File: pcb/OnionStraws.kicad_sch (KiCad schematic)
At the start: 33 parts, among them J1 8P8C, Q1 Si2393DS

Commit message: Updated PCB
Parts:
- C2: value 10u -> 100u
- C3: value 100n -> 1u
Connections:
- net GEA_HalfDplx: now also D?.2 (A); no longer D?.1 (K)
- net at R6.1, U?.12 (B2): now also D?.1 (K); no longer D?.2 (A)
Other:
- note added: "Add voltage supervisor to hold ESP reset until power is good."
- note added: "FullRX & TX not tested"
- moved on the sheet: D?
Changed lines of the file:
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@@
     (stroke (width 0) (type default) (color 0 0 0 0))
+  )
+  (text "Add voltage supervisor to hold ESP reset until power is good."
+    (at 85.725 191.77 0)
+    (effects (font (size 1.27 1.27)) (justify left bottom))
   )
   (text "EN" (at 256.54 35.56 0)
@@
   )
   (text "VI" (at 256.54 33.02 0)
+    (effects (font (size 1.27 1.27)) (justify left bottom))
+  )
+  (text "FullRX & TX not tested" (at 85.725 186.055 0)
     (effects (font (size 1.27 1.27)) (justify left bottom))
   )
@@
       (effects (font (size 1.27 1.27)) (justify left))
     )
-    (property "Value" "10u" (id 1) (at 242.951 44.958 0)
+    (property "Value" "100u" (id 1) (at 242.951 44.958 0)
       (effects (font (size 1.27 1.27)) (justify left))
     )
@@
       (effects (font (size 1.27 1.27)) (justify left))
     )
-    (property "Value" "100n" (id 1) (at 252.476 44.958 0)
+    (property "Value" "1u" (id 1) (at 252.476 44.958 0)
       (effects (font (size 1.27 1.27)) (justify left))
     )
@@
     (pin "8")
   )
-  (symbol (lib_id "Diode:1N4148") (at 235.585 114.3 270) (unit 1)
+  (symbol (lib_id "Diode:1N4148") (at 235.585 114.3 90) (unit 1)
     (in_bom yes) (on_board yes) (fields_autoplaced)
     (property "Reference" "D?" (id 0) (at 237.617 113.3915 90)
-      (effects (font (size 1.27 1.27)) (justify left))
+      (effects (font (size 1.27 1.27)) (justify right))
     )
     (property "Value" "1N4148" (id 1) (at 237.617 116.1666 90)
-      (effects (font (size 1.27 1.27)) (justify left))
-    )
-    (property "Footprint" "Diode_THT:D_DO-35_SOD27_P7.62mm_Horizontal" (id 2) (at 231.14 114.3 0)
+      (effects (font (size 1.27 1.27)) (justify right))
+    )
+    (property "Footprint" "Diode_THT:D_DO-35_SOD27_P7.62mm_Horizontal" (id 2) (at 240.03 114.3 0)
       (effects (font (size 1.27 1.27)) hide)
     )
@@
     )
     (path "/00000000-0000-0000-0000-00005f333718"
-      (reference "C2") (unit 1) (value "10u") (footprint "")
+      (reference "C2") (unit 1) (value "100u") (footprint "")
     )
     (path "/00000000-0000-0000-0000-00005f36c601"
-      (reference "C3") (unit 1) (value "100n") (footprint "")
+      (reference "C3") (unit 1) (value "1u") (footprint "")
     )
     (path "/00000000-0000-0000-0000-00005f3718ad"

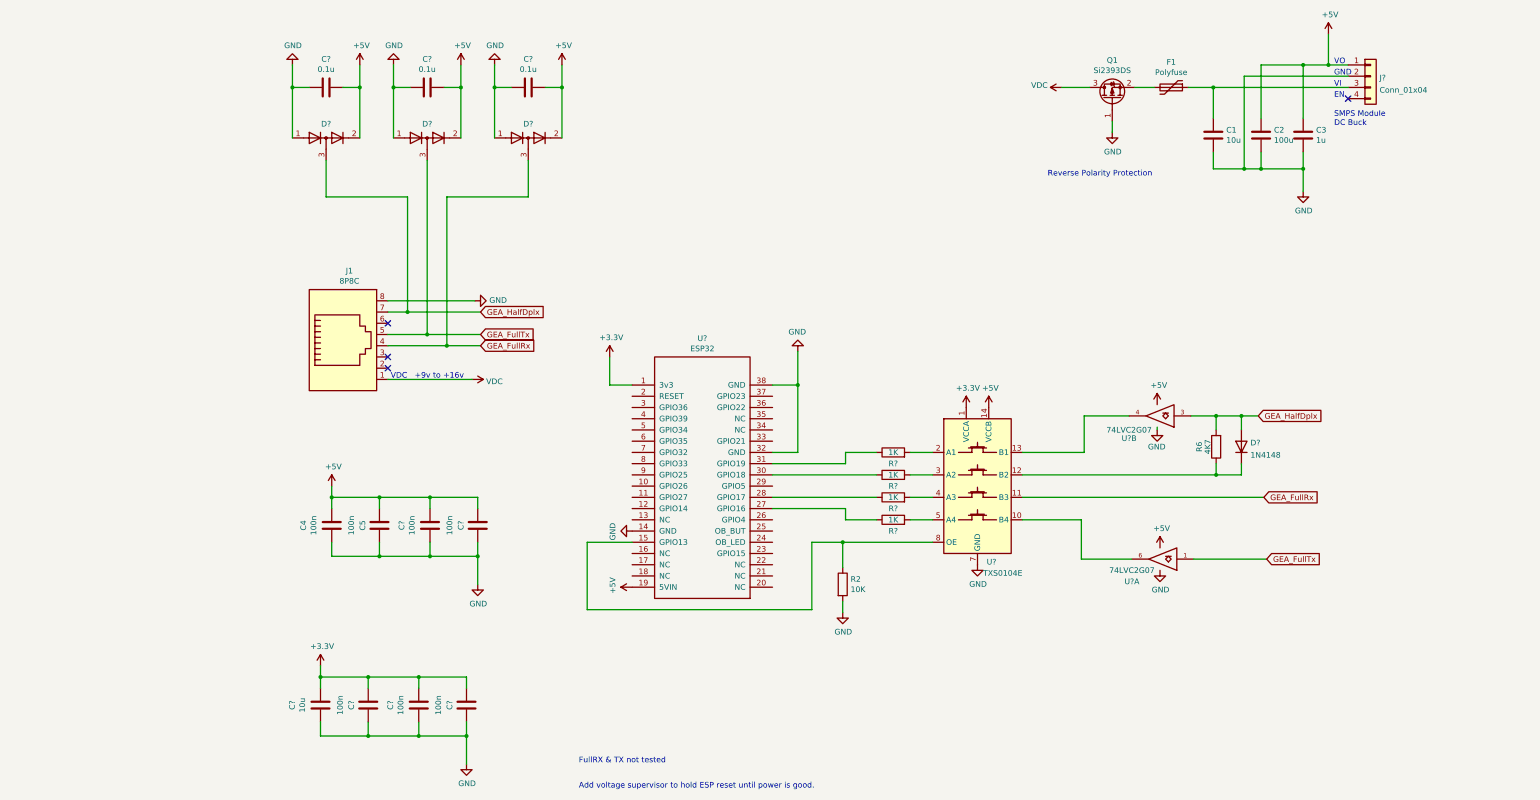
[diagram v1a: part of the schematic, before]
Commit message: Update PCB for full duplex
ESP tx to washer not tested yet
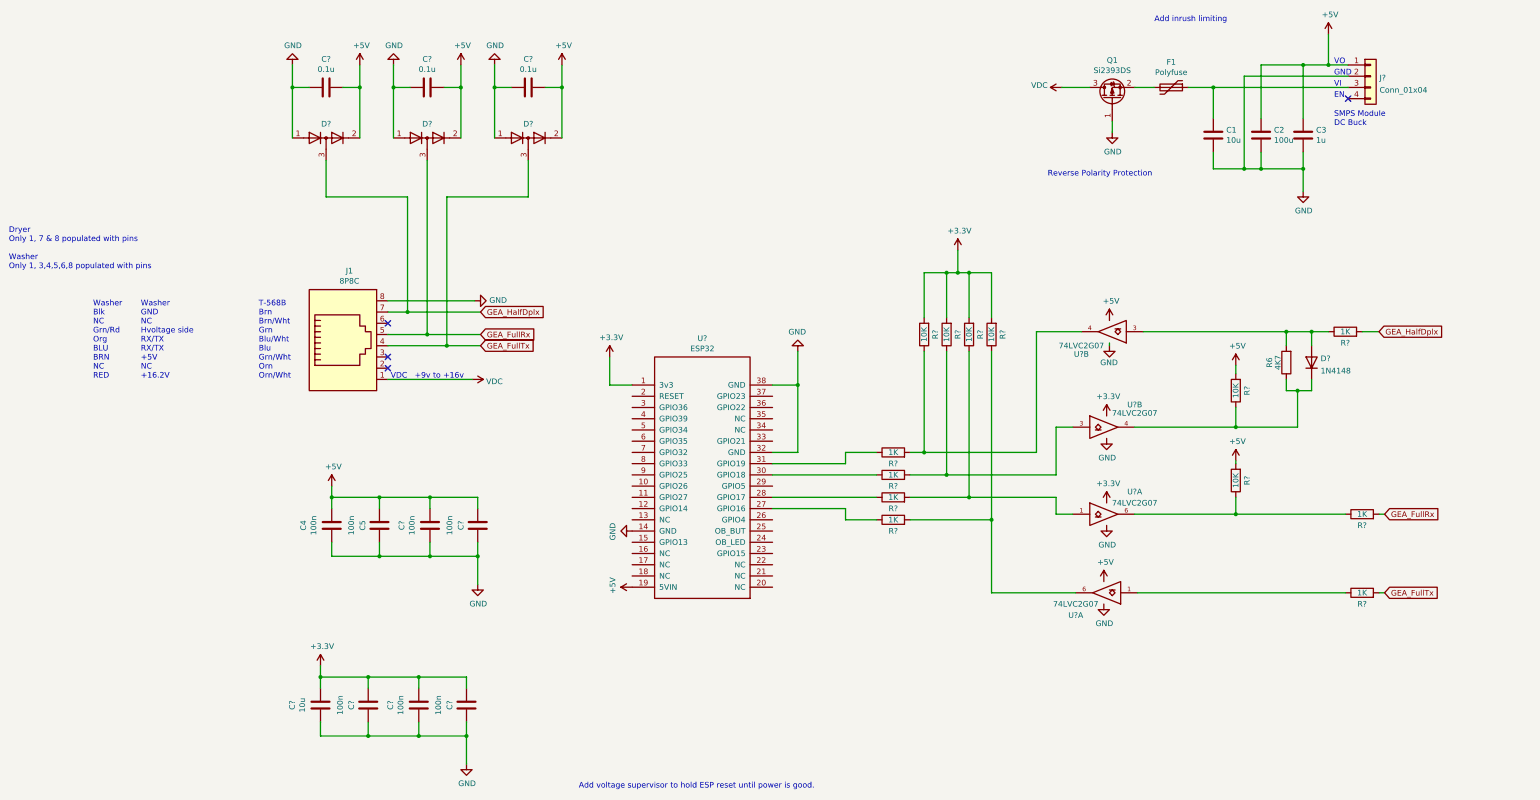
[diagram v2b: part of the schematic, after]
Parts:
- removed R2: 10K, symbol Device:R
- removed U?: TXS0104E, Housings_SSOP:TSSOP-14_4.4x5mm_Pitch0.65mm, symbol AtariWiiWifi:TXS0104E
- added R? (x6): 10K, symbol Device:R
- added R? (x3): 1K, symbol Device:R
- added U? (x2): 74LVC2G07, symbol 74xGxx:74LVC2G07
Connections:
- net +5V is gone; now on net +3V3: C1.2, C2.1, C2.2, C3.1, C3.2, C4.1, C4.2, C5.1, C5.2, C?.1, C?.1, C?.1, C?.1, C?.1, C?.1, C?.1, C?.2, C?.2, C?.2, C?.2, C?.2, C?.2, C?.2, D?.1 (K), D?.1 (K), D?.1 (K), D?.2 (A), D?.2 (A), D?.2 (A), J1.8, J?.1 (Pin_1), J?.2 (Pin_2), Q1.1 (G), U?.14 (GND), U?.19 (5VIN), U?.2 (GND), U?.2 (GND), U?.32 (GND), U?.38 (GND), U?.5 (VCC), U?.5 (VCC)
- net +3V3: now also R?.2, R?.2, R?.2, R?.2, R?.2, R?.2, U?.2 (GND), U?.2 (GND), U?.5 (VCC), U?.5 (VCC)
- net GEA_FullRx: now also D?.3 (K), J1.5, R?.2; no longer D?.3 (K), J1.4
- net GEA_FullTx: now also D?.3 (K), J1.4, R?.2; no longer D?.3 (K), J1.5, U?.1
- net GEA_HalfDplx: now also R?.2; no longer D?.2 (A), R6.2, U?.3
- net at R?.2: now also U?.6, R?.1
- net at D?.1 (K), R6.1: now also R?.1, U?.4
- net at U?.4: now also R?.2, R?.1
- net at R?.2: now also R?.1, U?.3
- net at R?.2: now also R?.1, U?.1
- new net: D?.2 (A), R6.2, R?.1, U?.3
- new net: R?.1, U?.1
- new net: R?.1, R?.1, U?.6
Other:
- note added: "Add inrush limiting"
- note added: "Dryer Only 1, 7 & 8 populated with pins Washer Only 1, 3,4,5,6,8 populated with pins"
- note added: "T-568B Brn Brn/Wht Grn Blu/Wht Blu Grn/Wht Orn Orn/Wht"
- note added: "Washer Blk NC Grn/Rd Org BLU BRN NC RED"
- note added: "Washer GND NC Hvoltage side RX/TX RX/TX +5V NC +16.2V"
- note removed: "FullRX & TX not tested"
- moved on the sheet: D?, R6, U?A, U?B

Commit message: Rev 0.1 of PCB
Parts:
- removed C? (x4): 100n, symbol Device:C
- removed D?: 1N4148, Diode_THT:D_DO-35_SOD27_P7.62mm_Horizontal, symbol Diode:1N4148
- removed JP1: WriteProtect, symbol Jumper:SolderJumper_2_Open
- removed U? (x2): 74LVC2G07, symbol 74xGxx:74LVC2G07
- added C4: 1u, Capacitor_SMD:C_0805_2012Metric, symbol Device:C
- added D4: BAV99, Package_TO_SOT_SMD:SOT-23, symbol Diode:BAV99
- added H1, H2, H3, H4: MountingHole, MountingHole:MountingHole_3.2mm_M3_DIN965, symbol Mechanical:MountingHole
- added Q1: Si2309CDS, Package_TO_SOT_SMD:SOT-23, symbol Device:Q_PMOS_GSD
- added R1: DNP, Resistor_SMD:R_0805_2012Metric, symbol Device:R
- added R17, R3: 250k, Resistor_SMD:R_0805_2012Metric, symbol Device:R
- added R2: 1M, Resistor_SMD:R_0805_2012Metric, symbol Device:R
- added U2: 74LVC2G07_3v3, Package_TO_SOT_SMD:SOT-23-6, symbol onionStraws:74LVC2G07_3v3
- added U4: APX803L, Package_TO_SOT_SMD:SOT-23, symbol onionStraws:APX803L
- C10, C11: renamed from C?; footprint (none) -> Capacitor_SMD:C_0805_2012Metric
- C5: renamed from C1; value 10u -> 100u; footprint (none) -> Capacitor_SMD:C_0805_2012Metric
- C6: renamed from C2; value 100u -> 10u; footprint (none) -> Capacitor_SMD:C_0805_2012Metric
- C7: renamed from C3; footprint (none) -> Capacitor_SMD:C_0805_2012Metric
- C8: renamed from C4; footprint (none) -> Capacitor_SMD:C_0805_2012Metric
- C9: renamed from C5; footprint (none) -> Capacitor_SMD:C_0805_2012Metric
- F1: footprint Resistors_SMD:R_1812_HandSoldering -> Resistor_SMD:R_1210_3225Metric_Pad1.30x2.65mm_HandSolder
- J1: renamed from J?; footprint (none) -> Connector_PinHeader_2.54mm:PinHeader_1x04_P2.54mm_Horizontal
- J2: renamed from J1; footprint Connectors:RJ45_8 -> Connector_RJ:RJ45_Amphenol_54602-x08_Horizontal
- Q2: renamed from Q1; value Si2393DS -> Si2309CDS; footprint (none) -> Package_TO_SOT_SMD:SOT-23
- R10, R11, R12, R13, R14, R15, R16, R18, R4, R6, R7, R8, R9: renamed from R?; footprint (none) -> Resistor_SMD:R_0805_2012Metric
- R5: renamed from R6; footprint (none) -> Resistor_SMD:R_0805_2012Metric
- U1: renamed from U?; footprint (none) -> Package_TO_SOT_SMD:SOT-23-6
- U3: renamed from U?; footprint AtariWiiWifi:DIP-38_900_ELL -> Library:DIP-38_900_ELL; symbol AtariWiiWifi:ESP32 -> onionStraws:ESP32
- gave numbers to parts that had none: 6
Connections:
- net +3V3: now also U2.5 (+3V3), U2.5 (+3V3); no longer C1.1, C1.2, C10.2, C11.1, C2.1, C2.2, C3.1, C3.2, C5.2, C6.1, C6.2, C7.1, C7.2, C8.1, C8.2, C9.1, C9.2, D1.1 (K), D1.2 (A), D2.1 (K), D2.2 (A), D3.1 (K), D3.2 (A), J1.1 (Pin_1), J1.2 (Pin_2), J2.8, Q2.1 (G), R10.2, R13.2, U1.2 (GND), U1.2 (GND), U1.5 (VCC), U1.5 (VCC), U3.14 (GND), U3.19 (5VIN), U3.32 (GND), U3.38 (GND)
- net VDC: now also F1.2; no longer Q2.3 (D)
- net p2: now reaches Q2.2 (S)
- net p2: now also C4.1, Q1.2 (S), R1.2; no longer F1.2
- net p3: now reaches C5.1, J1.3 (Pin_3)
- net p3: now also Q2.3 (D); no longer F1.1
- net at R10.1, R5.1: now also D4.3 (K), U2.6
- net at R4.1, R5.2, U1.3: now also D4.1 (K), R3.1
- net at R18.1, U1.1: now also R17.1
- net at U3.2 (EN): now also U4.2 (~{RESET})
- net at R14.2, R8.1: now also U2.3
- net at R13.1, R15.1: now also U2.4
- net at R12.2, R7.1: now also U2.1
- new net: C4.2, Q2.1 (G), R1.1, R2.2
- new net +5V: C1.1, C2.1, C3.1, C6.1, C7.1, C8.1, C9.2, D1.2 (A), D2.2 (A), D3.2 (A), J1.1 (Pin_1), R10.2, R13.2, R17.2, R3.2, U1.5 (VCC), U1.5 (VCC), U3.19 (5VIN), U4.3 (Vcc)
- new net GND: C1.2, C10.2, C11.1, C2.2, C3.2, C5.2, C6.2, C7.2, C8.2, C9.1, D1.1 (K), D2.1 (K), D3.1 (K), J1.2 (Pin_2), J2.8, Q1.1 (G), R2.1, U1.2 (GND), U1.2 (GND), U2.2 (GND), U2.2 (GND), U3.14 (GND), U3.32 (GND), U3.38 (GND), U4.1 (GND)
- new net p1: F1.1, Q1.3 (D)
- no-connect marks 4 -> 33
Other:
- note added: "Decoupling Caps"
- note added: "ESD Protection"
- note added: "Extra LED or PB?"
- note added: "Peak of 1.5 amps w/o inrush"
- note added: "Reverse polarity protection and inrush current limit"
- note added: "Voltage Supervisor, Hold ESP reset for 200ms after power reaches 5V. Prevent brownout at boot."
- note removed: "Add inrush limiting"
- note removed: "Add voltage supervisor to hold ESP reset until power is good."
- note removed: "Reverse Polarity Protection"
- moved on the sheet: C5, C8, C9, F1, Q2, R10, R13, R15, R18, R4, R5, R6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

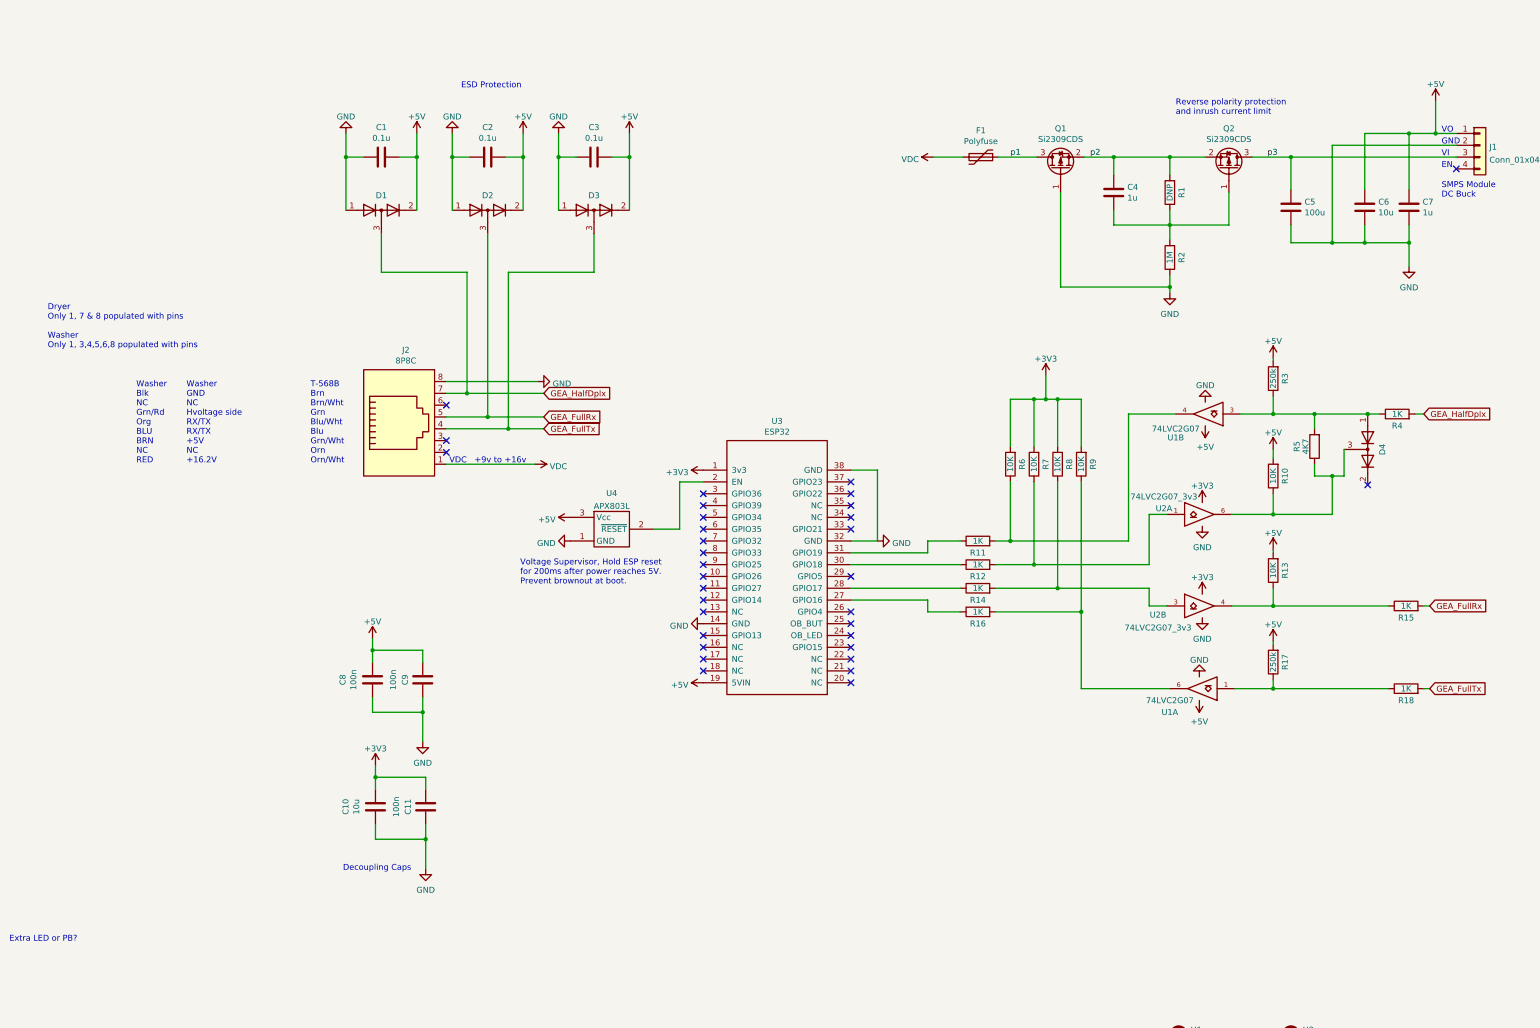
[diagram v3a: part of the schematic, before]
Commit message: PCB Rev 0.3
Fixed D4 and related pull up resistors.
Added LED and PB
Added 5V zener diode and TVS for input
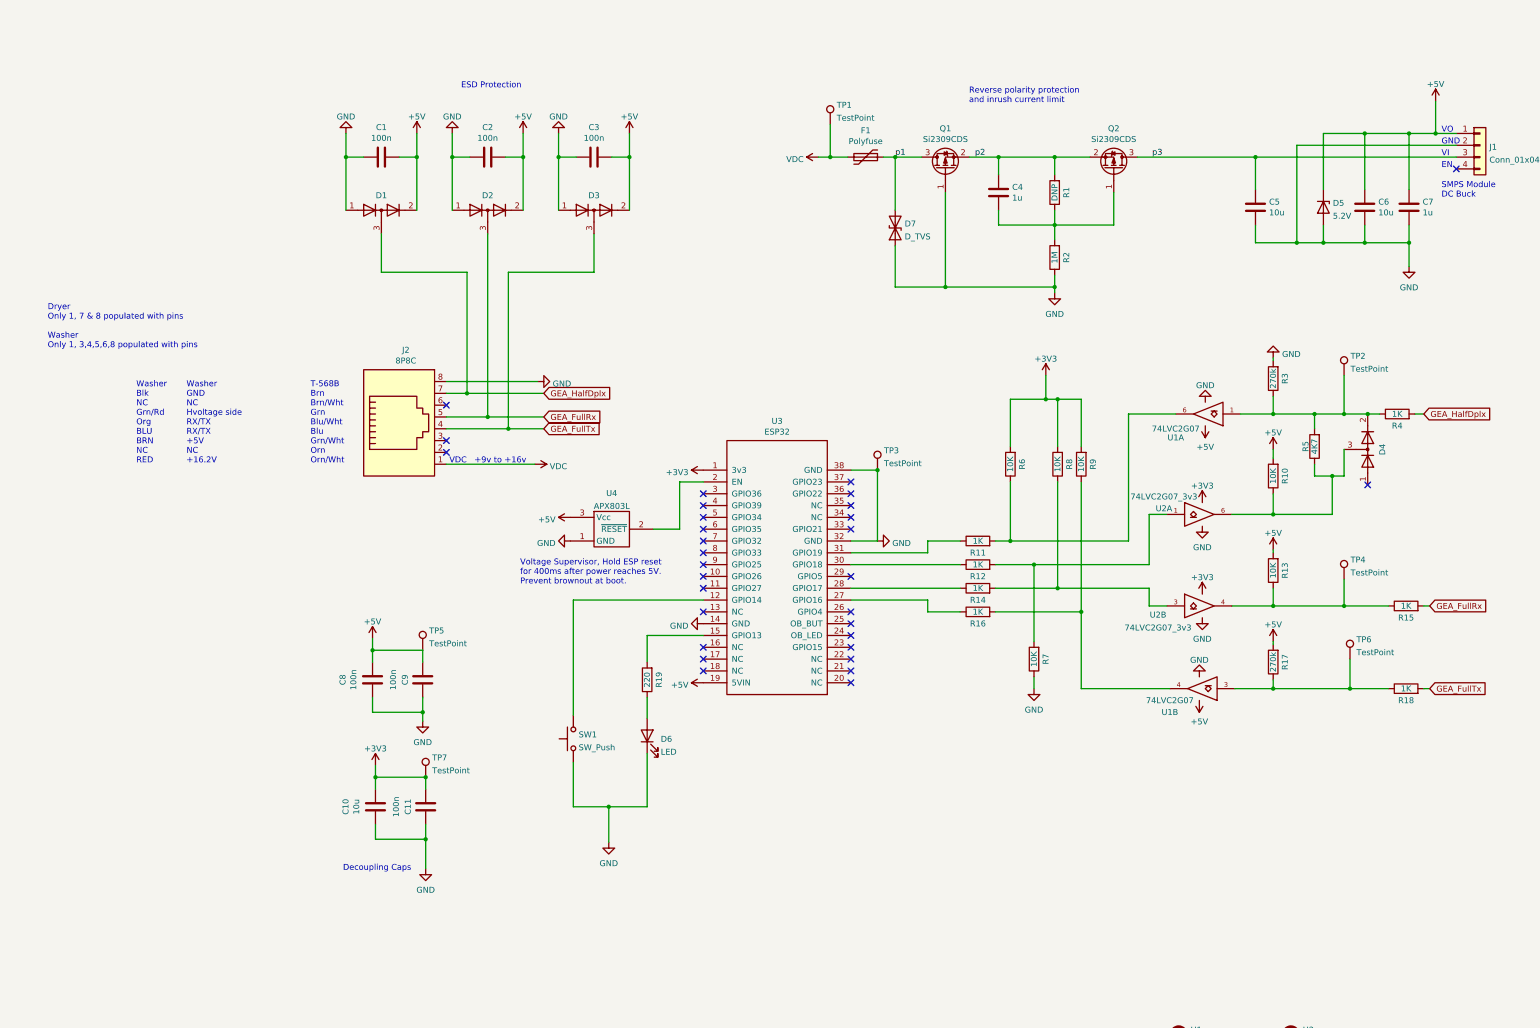
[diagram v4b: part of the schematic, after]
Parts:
- added D5: 5.2V, Diode_SMD:D_SOD-123, symbol Device:D_Zener
- added D6: LED, LED_THT:LED_D5.0mm, symbol Device:LED
- added D7: D_TVS, Diode_SMD:D_SMA, symbol Device:D_TVS
- added R19: 220, Resistor_SMD:R_0805_2012Metric, symbol Device:R
- added SW1: SW_Push, Button_Switch_THT:SW_PUSH_6mm_H13mm, symbol Switch:SW_Push
- added TP1, TP2, TP3, TP4, TP5, TP6, TP7: TestPoint, TestPoint:TestPoint_THTPad_D2.5mm_Drill1.2mm, symbol Connector:TestPoint
- C1, C2, C3: value 0.1u -> 100n
- C5: value 100u -> 10u
- R17, R3: value 250k -> 270k
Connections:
- net +3V3: now also TP7.1; no longer R7.2
- net +5V: now also D5.1 (K), TP5.1; no longer R3.2
- net GND: now also R3.2, R7.1, D5.2 (A), D6.1 (K), D7.1 (A1), SW1.1, TP3.1
- net VDC: now also TP1.1
- net p1: now also D7.2 (A2)
- net at R16.2, R9.1: now also U1.4; no longer U1.6
- net at R3.1, R4.1, R5.2: now also D4.2 (A), U1.1, TP2.1; no longer D4.1 (K), U1.3
- net at R17.1, R18.1: now also U1.3, TP6.1; no longer U1.1
- net at R11.2, R6.1: now also U1.6; no longer U1.4
- net at R13.1, R15.1, U2.4: now also TP4.1
- net at U3.12 (GPIO14): now also SW1.2
- net at U3.15 (GPIO13): now also R19.2
- net at R12.2, U2.1: now also R7.2; no longer R7.1
- new net: D6.2 (A), R19.1
- no-connect marks 33 -> 31
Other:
- note added: "Voltage Supervisor, Hold ESP reset for 400ms after power reaches 5V. Prevent brownout at boot."
- note removed: "Extra LED or PB?"
- note removed: "Voltage Supervisor, Hold ESP reset for 200ms after power reaches 5V. Prevent brownout at boot."
- title: (none) -> Onion Straws
- moved on the sheet: C4, C5, F1, Q1, Q2, R1, R2, R7

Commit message: PCB Rev 1.0
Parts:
- added R77: 270k, Resistor_SMD:R_0805_2012Metric, symbol Device:R
- added R88, R99: 10K, Resistor_SMD:R_0805_2012Metric, symbol Device:R
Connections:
- net GND: now also R77.2, R88.1, R99.1
- net at R16.2, R9.1, U1.4: now also R99.2
- net at R17.1, R18.1, TP6.1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: now also R77.1
- net at R14.2, R8.1, U2.3: now also R88.2
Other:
- moved on the sheet: R7
